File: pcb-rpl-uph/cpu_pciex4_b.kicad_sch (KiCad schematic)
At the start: 1 part, among them U5 RPL_UPH_FCBGA1744

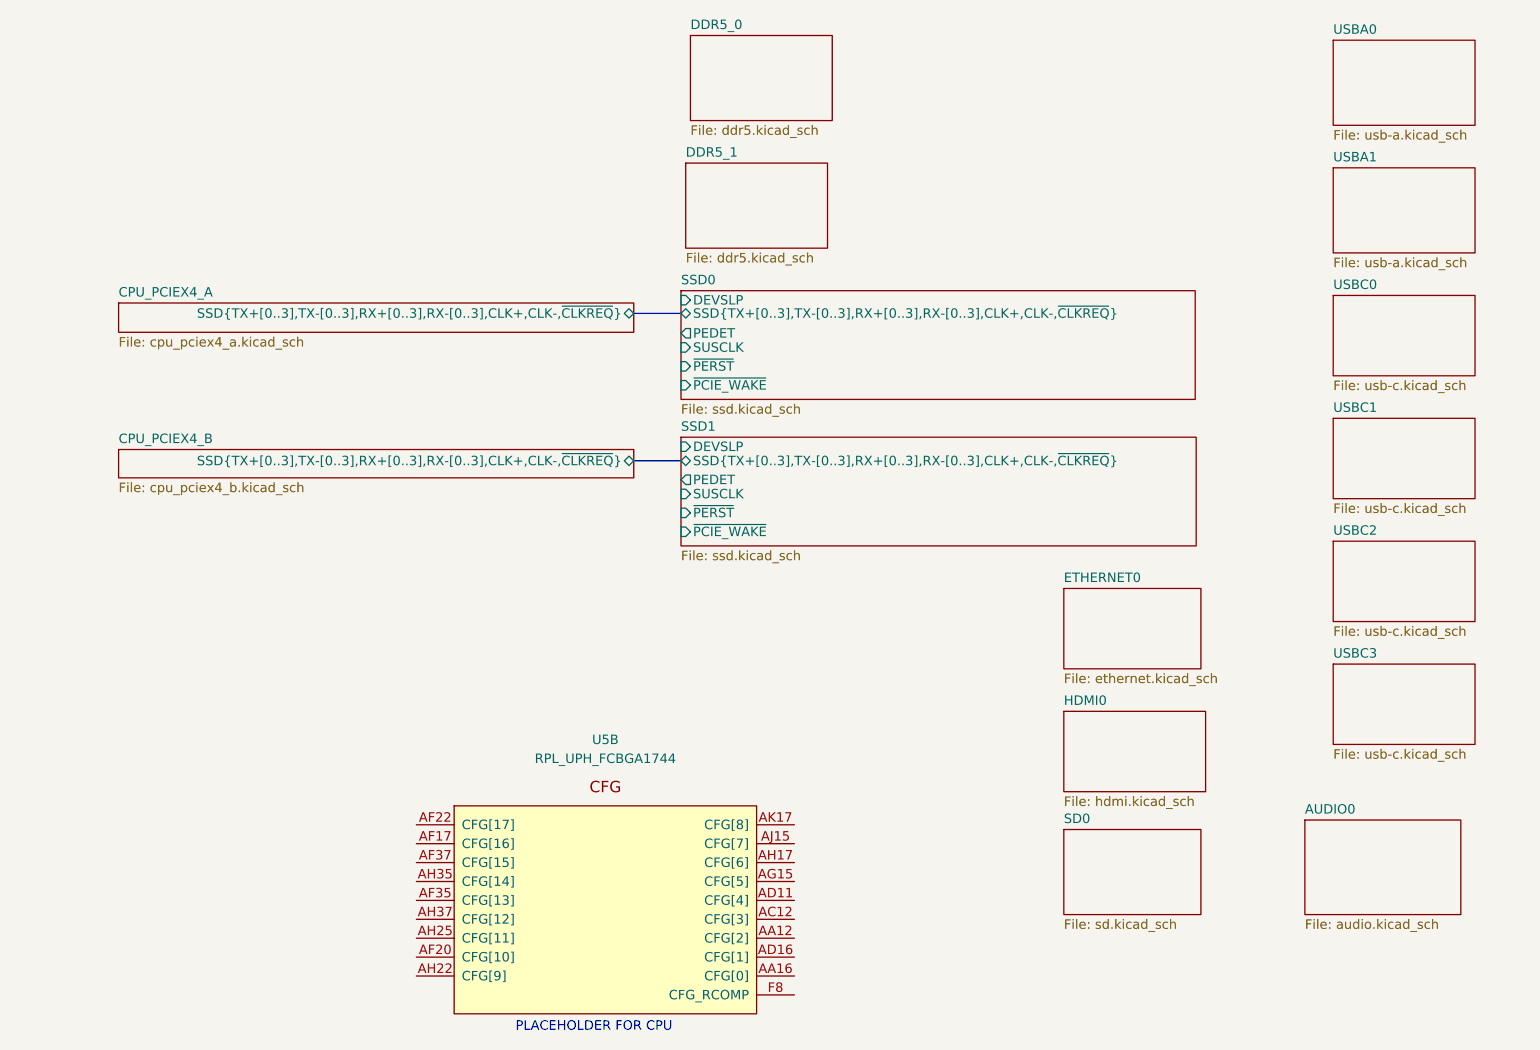
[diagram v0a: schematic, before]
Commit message: Connect SSD data signals
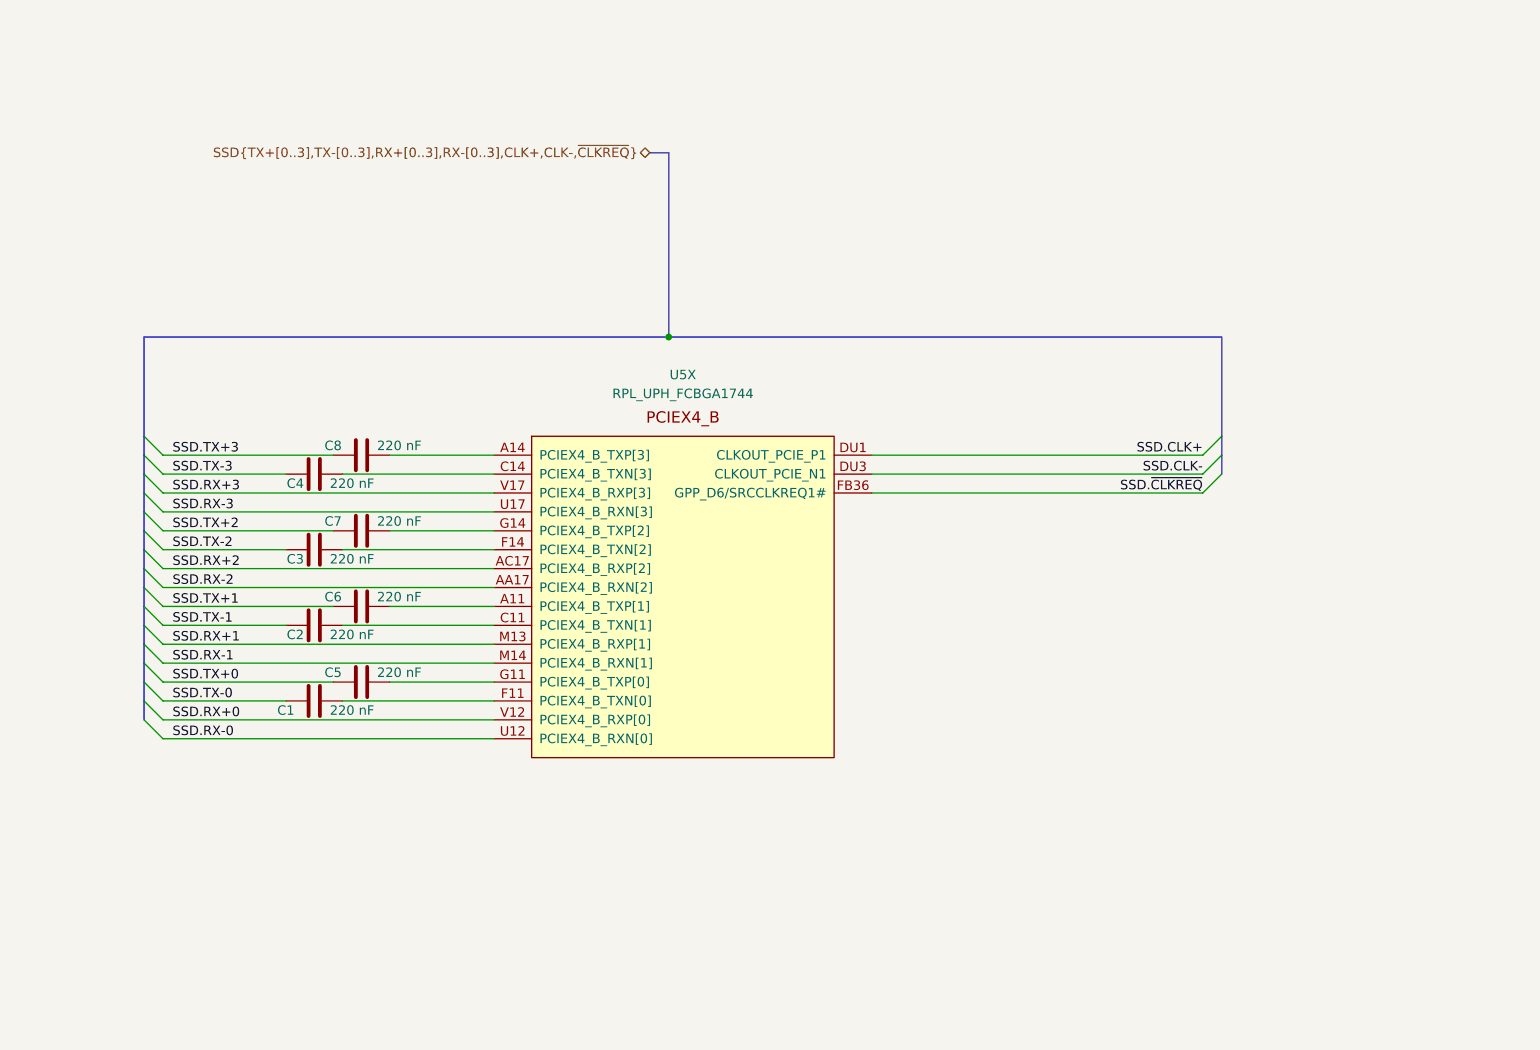
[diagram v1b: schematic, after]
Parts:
- removed U5: RPL_UPH_FCBGA1744, local:RPL_UPH_FCBGA1744, symbol local:RPL_UPH_FCBGA1744
- added C1, C2, C3, C4, C5, C6, C7, C8: 220 nF, local:C_0201_0603Metric, symbol Device:C
- added U5: RPL_UPH_FCBGA1744, symbol local:RPL_UPH_FCBGA1744
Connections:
- new net: C6.2, U5.A11 (PCIEX4_B_TXP[1])
- new net: C5.2, U5.G11 (PCIEX4_B_TXP[0])
- new net: C2.2, U5.C11 (PCIEX4_B_TXN[1])
- new net: C8.2, U5.A14 (PCIEX4_B_TXP[3])
- new net: C1.2, U5.F11 (PCIEX4_B_TXN[0])
- new net: C4.2, U5.C14 (PCIEX4_B_TXN[3])
- new net: C3.2, U5.F14 (PCIEX4_B_TXN[2])
- new net: C7.2, U5.G14 (PCIEX4_B_TXP[2])
- new net SSD.CLK+: U5.DU1 (CLKOUT_PCIE_P1)
- new net SSD.CLK-: U5.DU3 (CLKOUT_PCIE_N1)
- new net SSD.RX+0: U5.V12 (PCIEX4_B_RXP[0])
- new net SSD.RX+1: U5.M13 (PCIEX4_B_RXP[1])
- new net SSD.RX+2: U5.AC17 (PCIEX4_B_RXP[2])
- new net SSD.RX+3: U5.V17 (PCIEX4_B_RXP[3])
- new net SSD.RX-0: U5.U12 (PCIEX4_B_RXN[0])
- new net SSD.RX-1: U5.M14 (PCIEX4_B_RXN[1])
- new net SSD.RX-2: U5.AA17 (PCIEX4_B_RXN[2])
- new net SSD.RX-3: U5.U17 (PCIEX4_B_RXN[3])
- new net SSD.TX+0: C5.1
- new net SSD.TX+1: C6.1
- new net SSD.TX+2: C7.1
- new net SSD.TX+3: C8.1
- new net SSD.TX-0: C1.1
- new net SSD.TX-1: C2.1
- new net SSD.TX-2: C3.1
- new net SSD.TX-3: C4.1
- new net SSD.~{CLKREQ}: U5.FB36 (GPP_D6/SRCCLKREQ1#)
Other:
- removed sheet AUDIO0
- removed sheet CPU_PCIEX4_A
- removed sheet CPU_PCIEX4_B
- removed sheet DDR5_0
- removed sheet DDR5_1
- removed sheet ETHERNET0
- removed sheet HDMI0
- removed sheet SD0
- removed sheet SSD0
- removed sheet SSD1
- removed sheet USBA0
- removed sheet USBA1
- removed sheet USBC0
- removed sheet USBC1
- removed sheet USBC2
- removed sheet USBC3
- note removed: "PLACEHOLDER FOR CPU"

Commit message: Remove extra DC block caps on M.2 PCIe signals
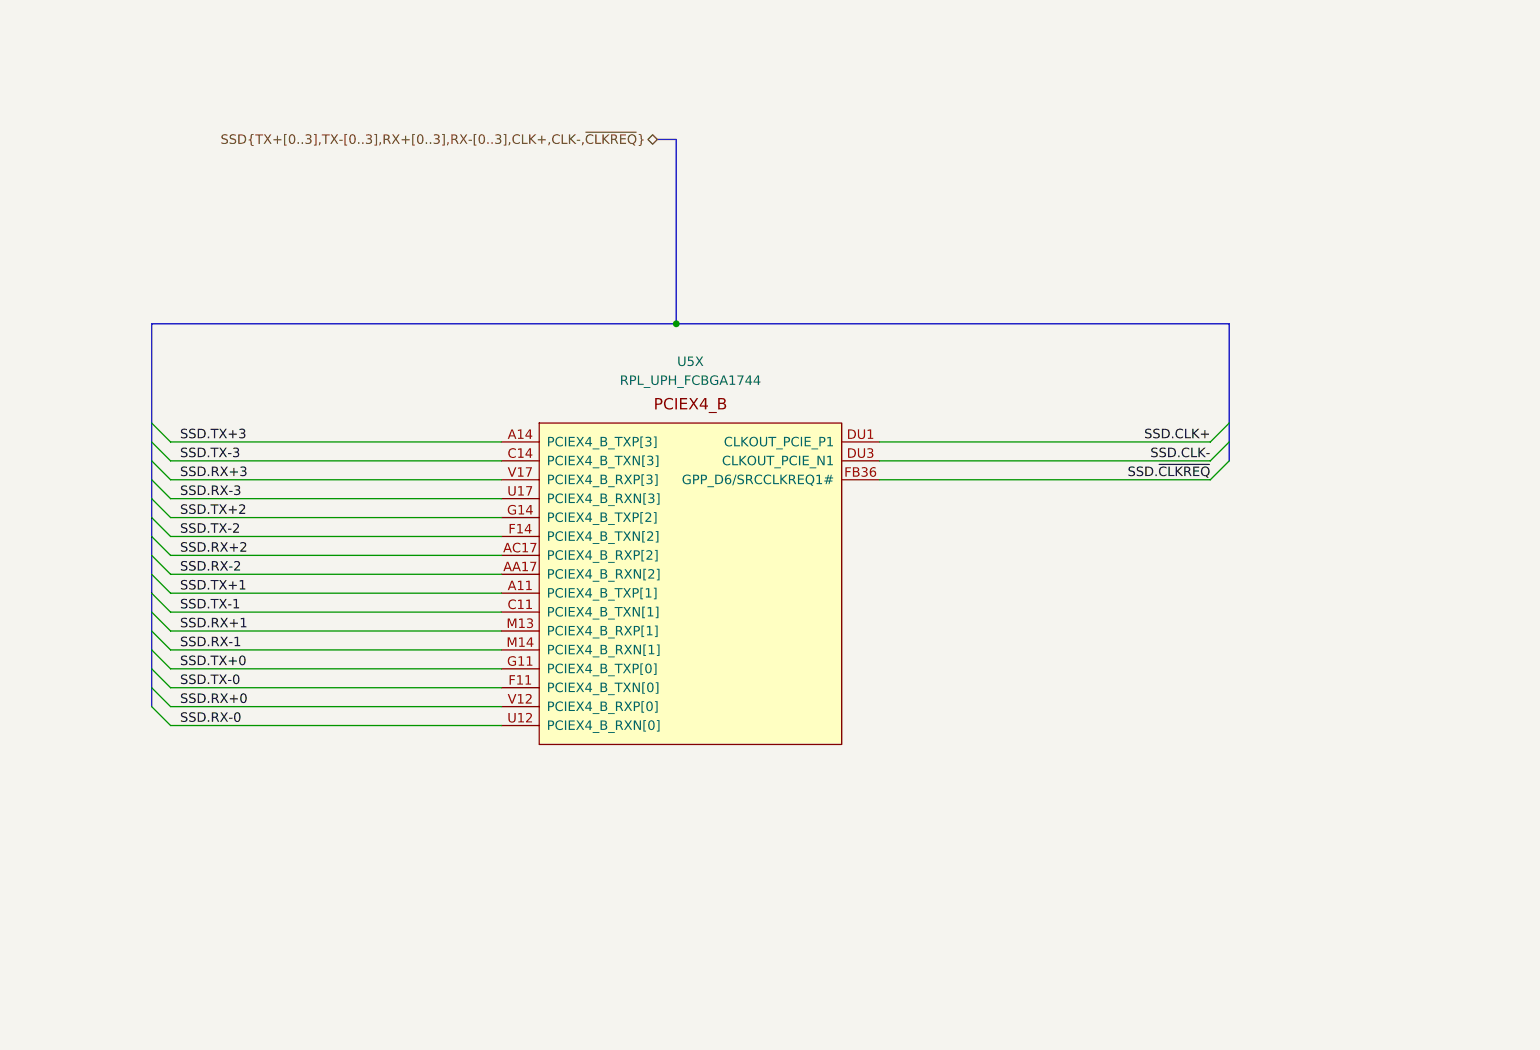
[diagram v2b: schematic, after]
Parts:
- removed C1, C2, C3, C4, C5, C6, C7, C8: 220 nF, local:C_0201_0603Metric, symbol Device:C
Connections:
- net SSD.TX+0: now also U5.G11 (PCIEX4_B_TXP[0])
- net SSD.TX+1: now also U5.A11 (PCIEX4_B_TXP[1])
- net SSD.TX+2: now also U5.G14 (PCIEX4_B_TXP[2])
- net SSD.TX+3: now also U5.A14 (PCIEX4_B_TXP[3])
- net SSD.TX-0: now also U5.F11 (PCIEX4_B_TXN[0])
- net SSD.TX-1: now also U5.C11 (PCIEX4_B_TXN[1])
- net SSD.TX-2: now also U5.F14 (PCIEX4_B_TXN[2])
- net SSD.TX-3: now also U5.C14 (PCIEX4_B_TXN[3])
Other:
- moved on the sheet: U5X

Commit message: add display connector
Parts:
- U5: footprint (none) -> local:RPL_UPH_FCBGA1744
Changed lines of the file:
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@@
       (effects (font (size 1.27 1.27)))
     )
-    (property "Footprint" "" (at 143.51 63.5 0)
+    (property "Footprint" "local:RPL_UPH_FCBGA1744" (at 143.51 63.5 0)
       (effects (font (size 1.27 1.27)) hide)
     )
